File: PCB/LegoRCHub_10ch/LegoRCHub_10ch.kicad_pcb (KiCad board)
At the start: 2 copper layers, 39.3 x 55.2 mm, 47 parts, among them J1 Conn_01x02, J10 Conn_01x03, J11 Conn_01x03_MountingPin, J12 Conn_01x02, J13 Conn_01x01, J2 Conn_01x02, J3 Conn_01x02, J4 Conn_01x02, J5 Conn_01x02, J6 Conn_01x02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

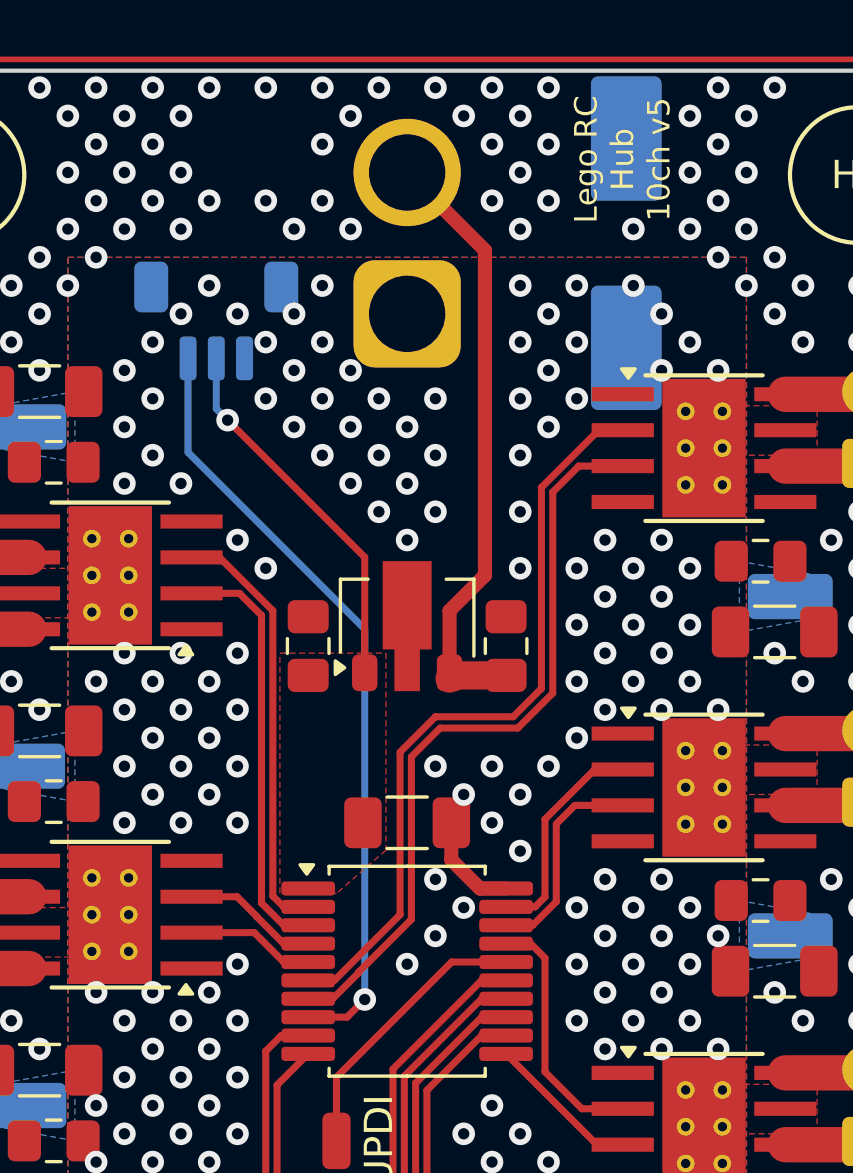
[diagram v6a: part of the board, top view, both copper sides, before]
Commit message: PCB v6: inverted connector (as it should be)
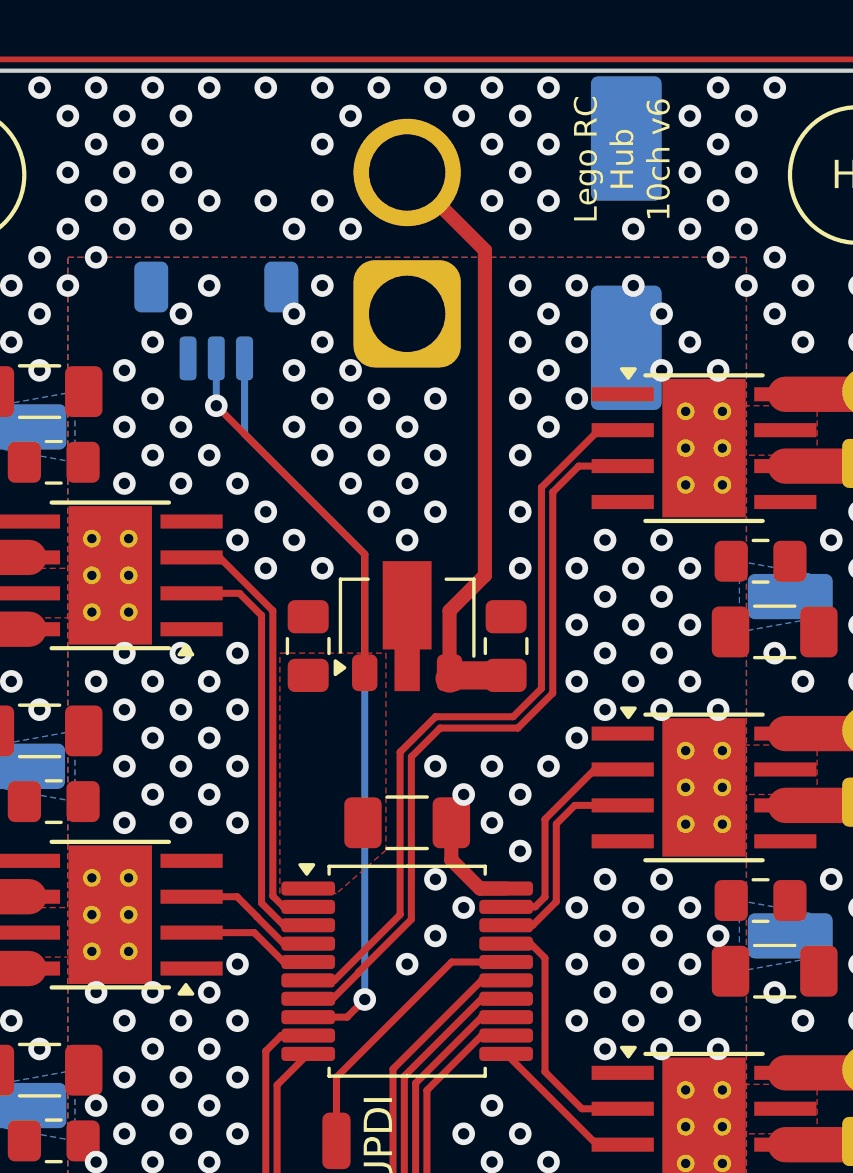
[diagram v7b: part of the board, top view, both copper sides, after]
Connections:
- J11 pad 1: GND -> /IBus
- J11 pad 3: /IBus -> GND
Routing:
- net /IBus: track 27.5 -> 26.7 mm
- net GND: vias 205 -> 208
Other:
- board text added: "+13V MAX"
- board text added: "Lego RC Hub 10ch v6"
- board text removed: "+12V MAX"
- board text removed: "Lego RC Hub 10ch v5"

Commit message: PCB: working on double CPU design...
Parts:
- added C23: 100nF, Capacitor_SMD:C_1206_3216Metric_Pad1.33x1.80mm_HandSolder, F.Cu at (44.5, 57.9)
- added J14: Conn_01x01, Connector_Wire:SolderWirePad_1x01_SMD_1x2mm, F.Cu at (44.5, 54.4)
- added U9: ATtiny3226-X, Package_SO:SSOP-20_5.3x7.2mm_P0.65mm, F.Cu at (44.5, 63.0)
- moved J13 6.98 mm to (44.5, 67.6), turned to -90 degrees
- moved U7 5.27 mm to (44.5, 49.8)
- moved C13 5.10 mm to (44.5, 44.7)
- moved C14 4.45 mm to (48.0, 39.1)
- moved C15 4.45 mm to (41.0, 39.1)
- moved U8 4.45 mm to (44.5, 38.1)
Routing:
- net /CH2_3: track 26.5 -> 2.86 mm
- net /CH2_2: track 25.9 -> 2.86 mm
- net /CH7: track 28.4 -> 8.05 mm
- net /CH9: track 23.0 -> 3.36 mm
- net /CH10: track 22.1 -> 3.07 mm
- net /CH8: track 25.9 -> 7.78 mm
- net /IBus: track 26.7 -> 8.69 mm, vias 1 -> 0
- net /CH1_2: track 14.9 -> 2.80 mm
- net VCC: track 13.5 -> 1.67 mm, vias 1 -> 2
- net +BATT: track 21.6 -> 10.1 mm
- net /CH1_3: track 15.2 -> 3.66 mm
- net /UPDI: track 9.94 -> 0.00 mm
- net /CH5_2: track 9.07 -> 0.00 mm
- net /CH5_3: track 10.2 -> 1.51 mm
- net /CH6_2: track 8.90 -> 1.44 mm
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- removed copper zone on F.Cu, net VCC
